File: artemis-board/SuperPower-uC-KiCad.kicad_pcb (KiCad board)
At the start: 4 copper layers, 45.1 x 45.1 mm, 87 parts, among them J1 Battery connector, J10 External NTC, J2 Thermistor, J3 USB_B_Micro, J4 Solar in, J7 DNP, J8 regulator board, Q1 2N7002, Q10 AO3401A, Q2 2N7002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

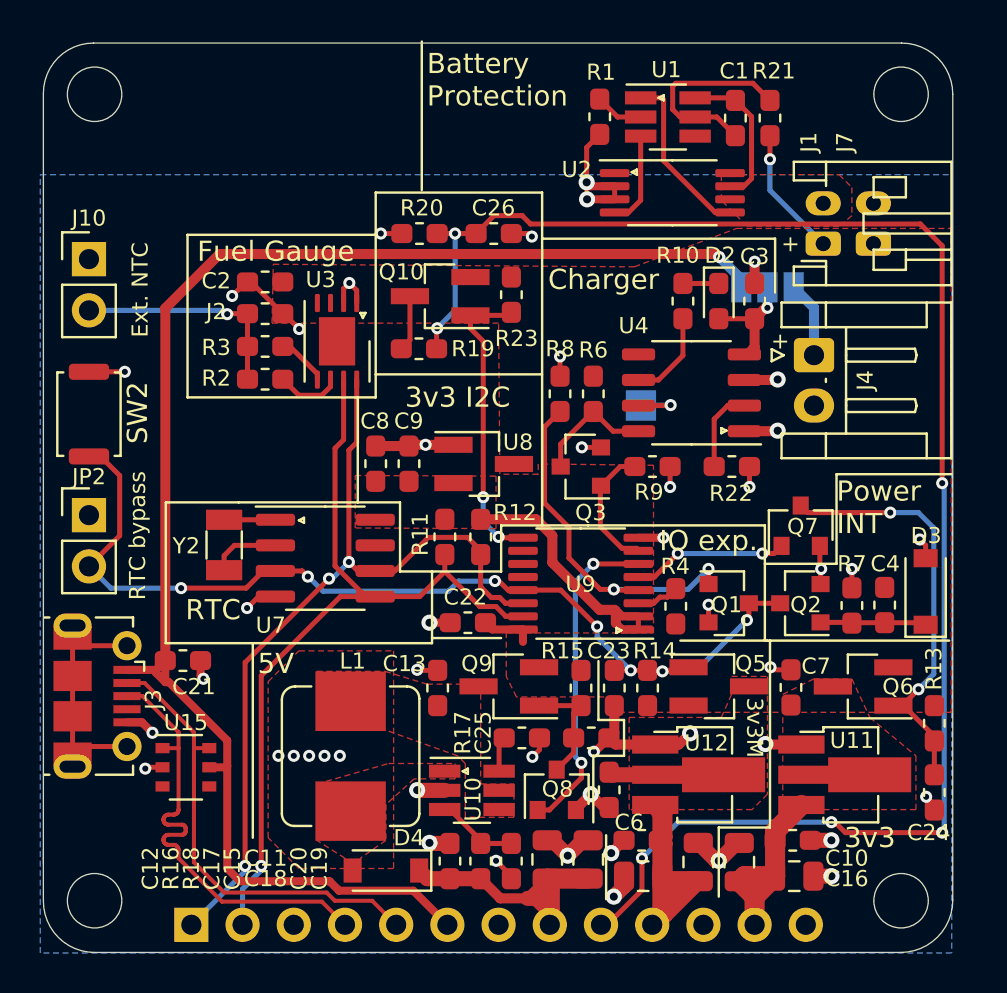
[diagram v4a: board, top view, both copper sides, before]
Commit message: moved R8 and did some minor silk and routing changes
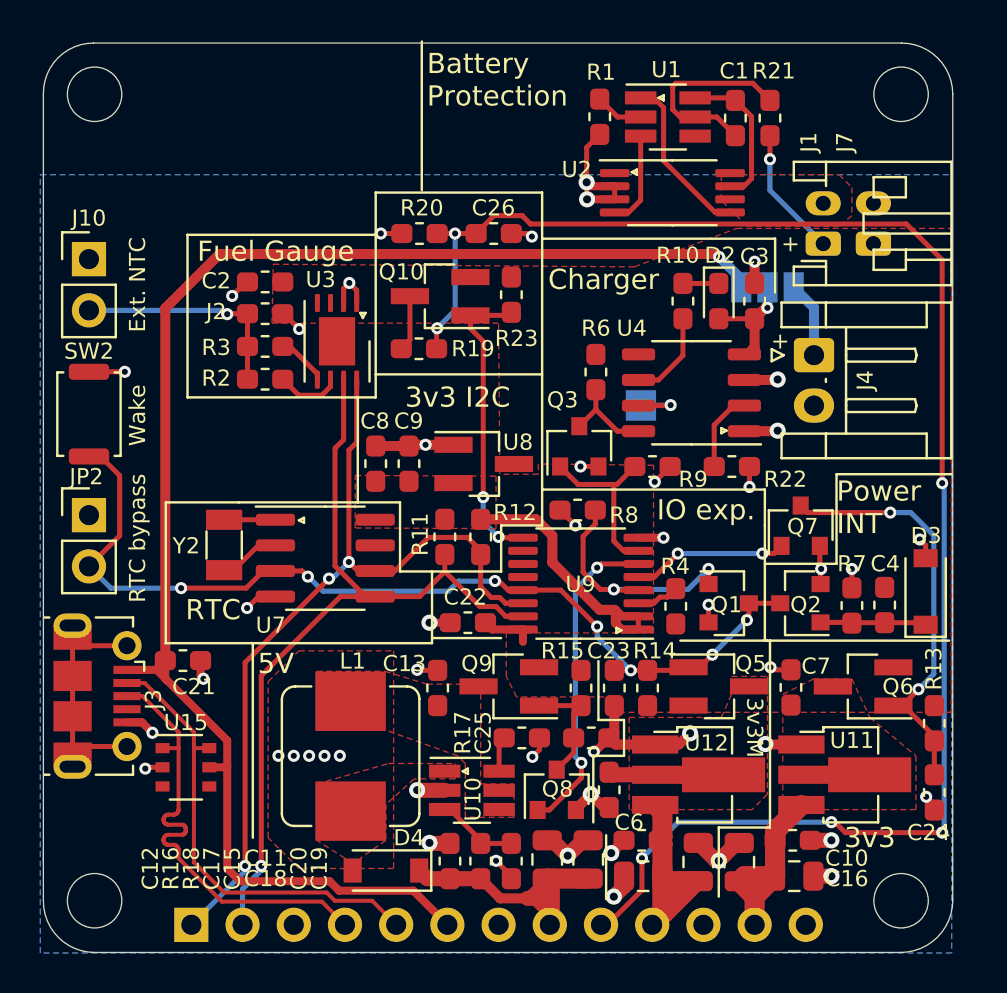
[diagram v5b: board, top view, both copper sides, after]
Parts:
- moved R8 5.83 mm to (159.7, 101.5), turned to 0 degrees
- moved R6 1.09 mm to (160.6, 94.6)
- moved Q3 1.01 mm to (159.8, 98.3), turned to 90 degrees
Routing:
- net /RTC and Cut-Off Module/~INT: track 18.1 -> 12.3 mm
- net GND: track 70.7 -> 68.6 mm
- net /RTC and Cut-Off Module/~CH_DIS: track 6.60 -> 8.67 mm
- net /Charging Module/INT: track 49.0 -> 47.5 mm
- net /Charging Module/CHARGE-DISABLE: track 6.05 -> 4.71 mm
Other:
- board text added: "Wake"

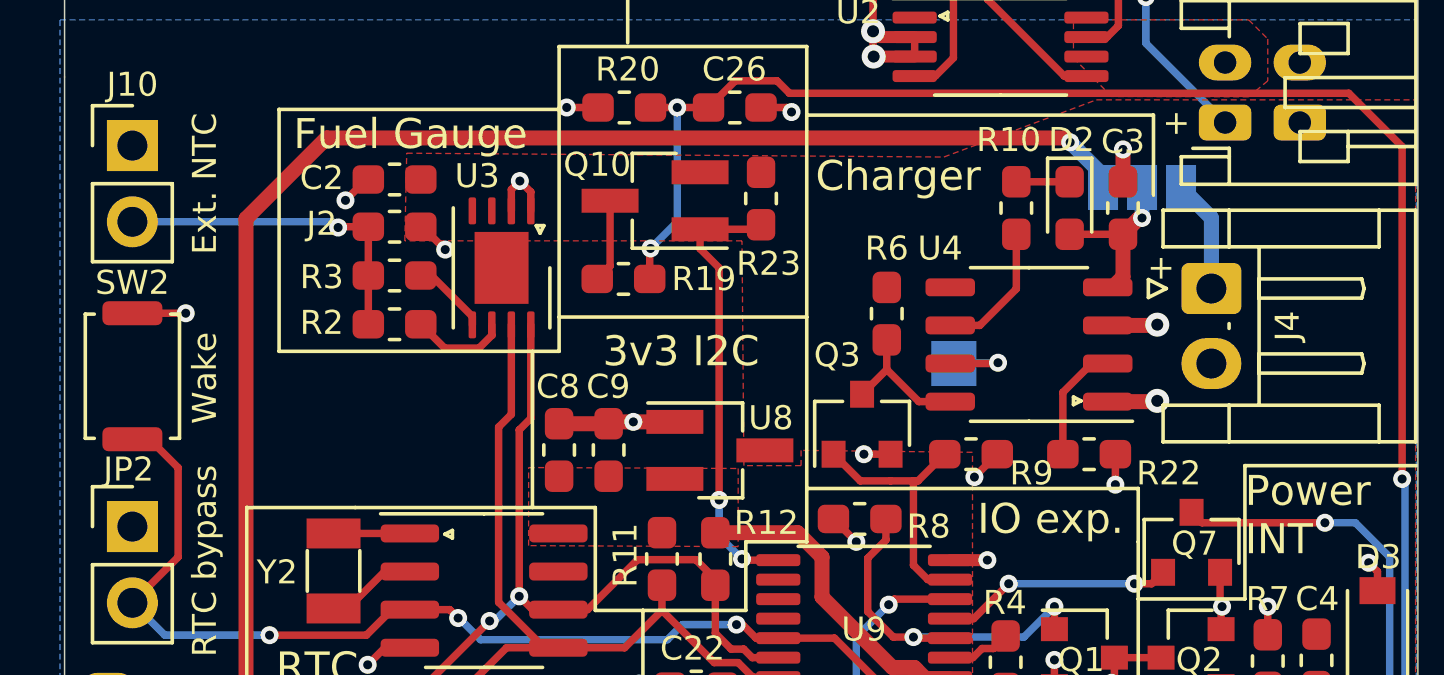
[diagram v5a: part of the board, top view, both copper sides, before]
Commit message: added comments and swapped polarity of Vin connector
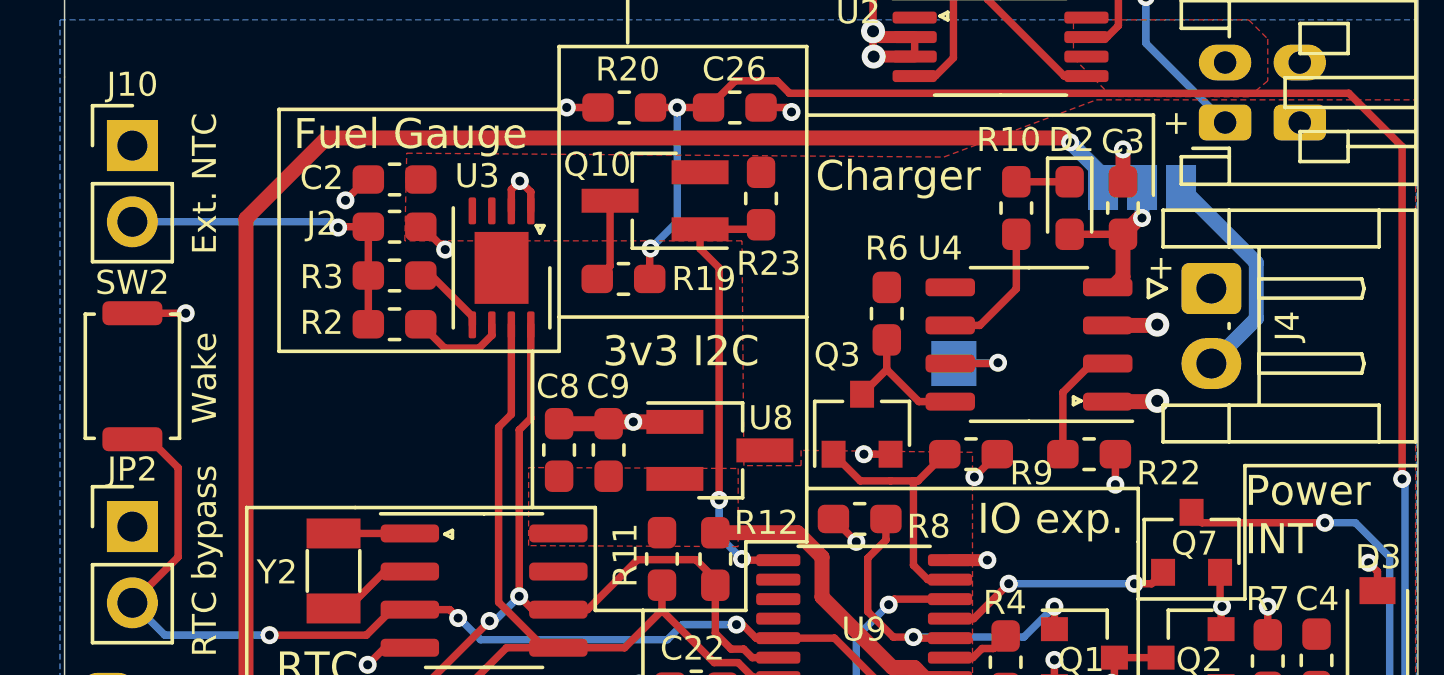
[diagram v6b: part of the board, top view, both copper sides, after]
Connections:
- J4 pad 1: Net-(J4-Pad1) -> GND
- J4 pad 2: GND -> Net-(J4-Pad2)
- JP1 pad 1: Net-(J4-Pad1) -> Net-(J4-Pad2)
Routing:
- net Net-(J4-Pad2): track 0.00 -> 7.71 mm
- net Net-(J4-Pad1): track 3.79 -> 0.00 mm

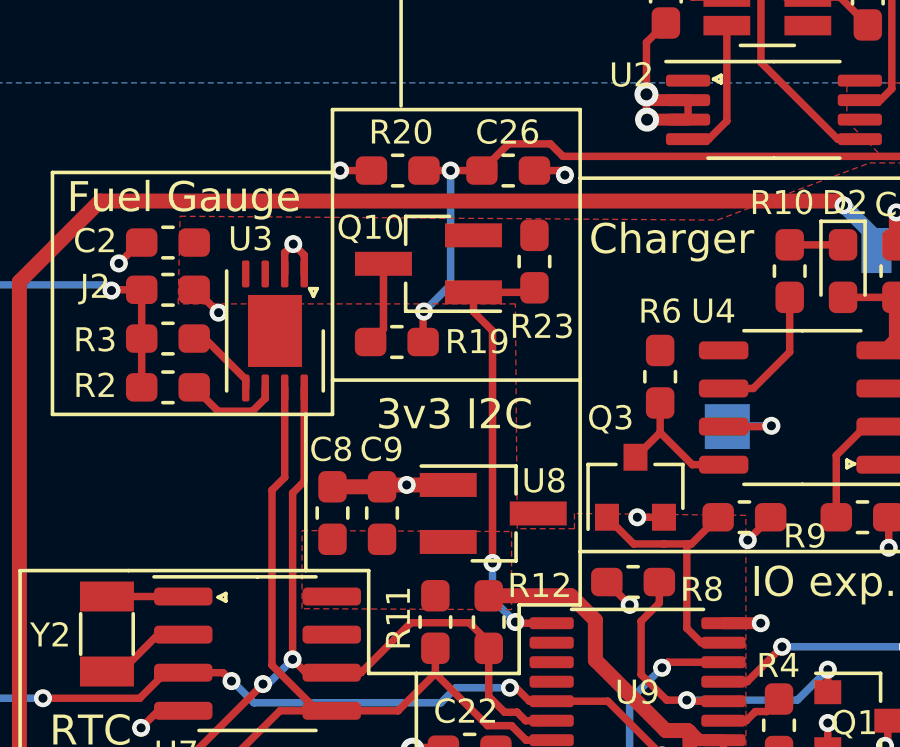
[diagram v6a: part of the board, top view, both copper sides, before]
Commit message: added 1µ cap close to 3v3 I2C regulator
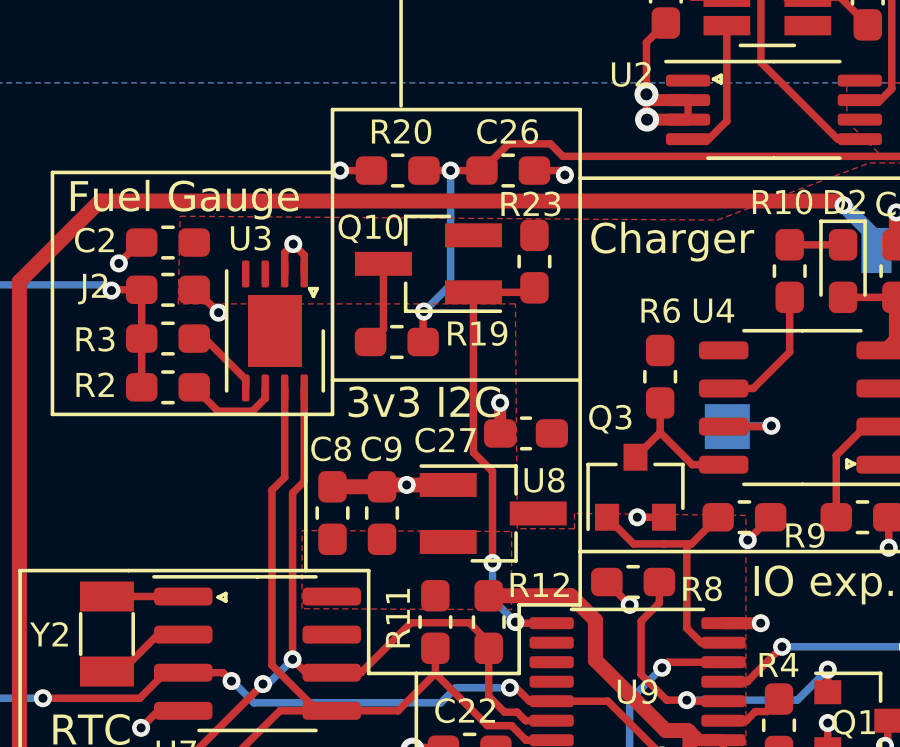
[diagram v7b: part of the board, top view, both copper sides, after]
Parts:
- added C27: 1µF, Capacitor_SMD:C_0603_1608Metric_Pad1.08x0.95mm_HandSolder, F.Cu at (156.2, 96.5)
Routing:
- net GND: track 68.4 -> 69.4 mm, vias 48 -> 49

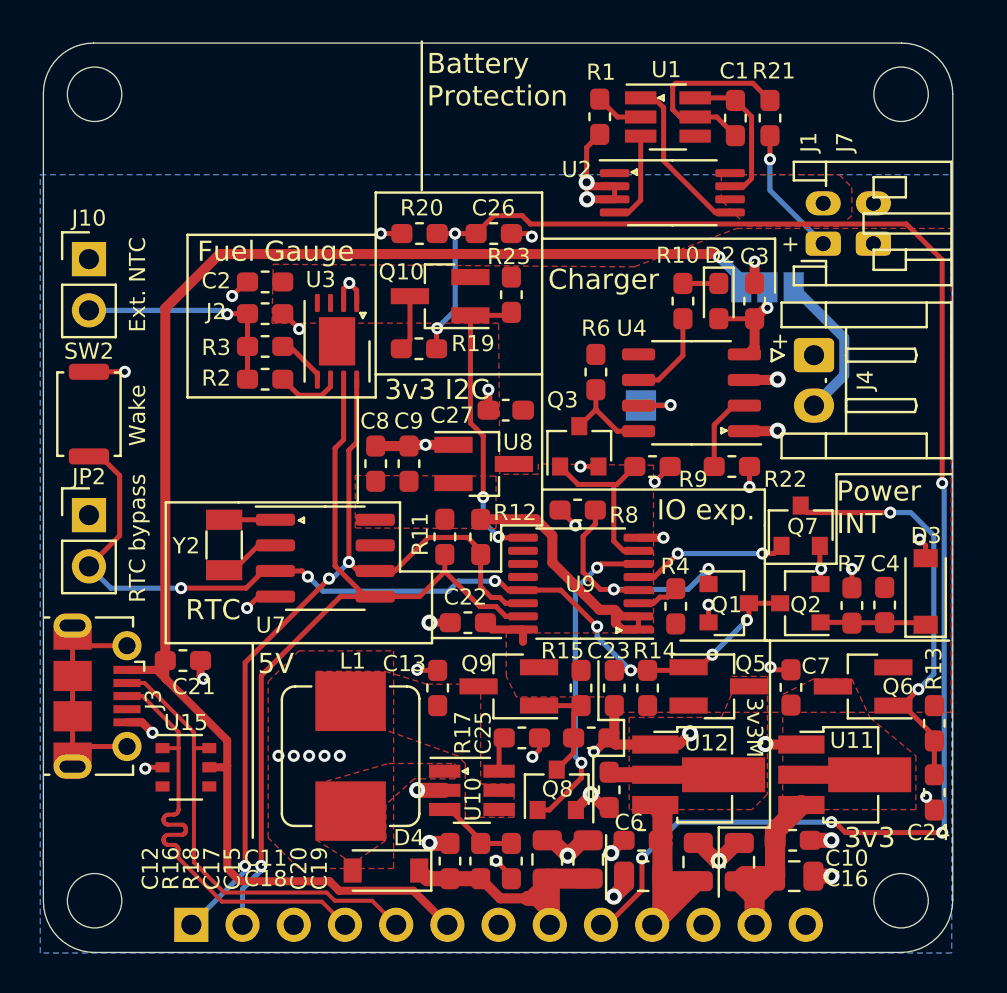
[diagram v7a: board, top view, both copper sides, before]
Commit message: swapped and added some lcsc part numbers and DNP markers
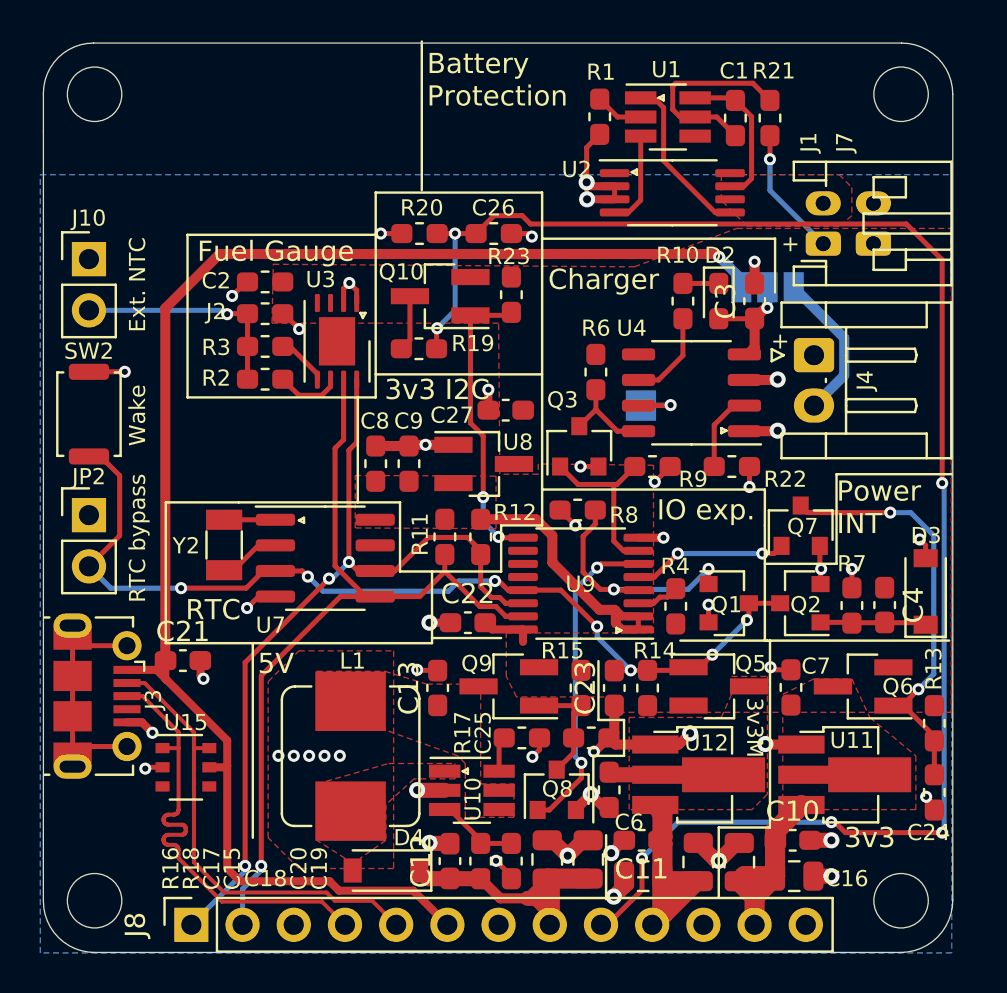
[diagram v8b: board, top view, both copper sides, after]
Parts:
- C10, C11, C12, C13, C21, C22, C23, C3, C4: footprint Capacitor_SMD:C_0603_1608Metric_Pad1.05x0.95mm_HandSolder -> Capacitor_SMD:C_0603_1608Metric_Pad1.08x0.95mm_HandSolder
- J7: value DNP -> unprotected BAT in
- J8: footprint Connector_PinHeader_2.54mm:PinHeader_1x13_P2.54mm_Vertical -> Connector_PinSocket_2.54mm:PinSocket_1x13_P2.54mm_Vertical; moved to F.Cu
- U3: value LC709203FQH -> LC709203FQH-01TWG
- turned J8 to 90 degrees
